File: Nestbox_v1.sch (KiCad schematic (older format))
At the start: 33 parts, among them P1 RX/TX, P2 TST/RST, P3 VDD/GND, Q1 SFH 3605, Q2 SFH 3605, SW1 SMD-BUTTON_2P-3.0X2.5X1.2+0.4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, U1 MSP430FR5969, Y1 Crystal

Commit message: updated schematics and BOM with MPN
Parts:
- D1: MPN (none) -> 720-SFH4646Z
- Q1, Q2: MPN (none) -> SFH 3605-Z
- RV1, RV2: MPN (none) -> 3313J-1-201E
- SW1: MPN B3U-1000P-2P-SMD -> B3U-1000P-B
- U1: MPN (none) -> MSP430FR5969IRGZR
- Y1: MPN (none) -> FC-12M 32.7680KA-A3
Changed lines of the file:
@@
 F 2 "chips:S-PVQFN-N48" H 4500 3500 60  0001 C CNN
 F 3 "" H 4500 3500 60  0001 C CNN
+F 4 "MSP430FR5969IRGZR" H 4500 3500 60  0001 C CNN "MPN"
+F 5 "" H 4500 3500 60  0001 C CNN "SKU"
+F 6 "" H 4500 3500 60  0001 C CNN "MouserLink"
 	1    4450 3650
 	1    0    0    -1
@@
 F 2 "Socket_Strips:Socket_Strip_Straight_1x02" H 5650 6450 50  0001 C CNN
 F 3 "" H 5650 6450 50  0000 C CNN
+F 4 "" H 5650 6450 50  0001 C CNN "MPN"
+F 5 "" H 5650 6450 50  0001 C CNN "SKU"
+F 6 "" H 5650 6450 50  0001 C CNN "MouserLink"
 	1    5650 6450
 	0    1    1    0
@@
 F 2 "SeeedOPL-Crystal Oscillator-2016:X2-SMD-L2.0X1.2X0.55MM" H 4150 1300 50  0001 C CNN
 F 3 "" H 4150 1300 50  0000 C CNN
+F 4 "FC-12M 32.7680KA-A3" H 4150 1300 50  0001 C CNN "MPN"
+F 5 "" H 4150 1300 50  0001 C CNN "SKU"
+F 6 "" H 4150 1300 50  0001 C CNN "MouserLink"
 	1    4150 1300
 	1    0    0    -1
@@
 F 3 "" H 3550 1350 60  0001 C CNN
 F 4 "303030020" H 3580 1500 20  0001 C CNN "SKU"
+F 6 "" H 3580 1500 20  0001 C CNN "" "MouserLink"
 	1    3550 1350
 	0    -1   -1   0
@@
 F 2 "Octanis3:MIDLED" H 650 4250 50  0001 C CNN
 F 3 "" H 650 4250 50  0000 C CNN
+F 4 "720-SFH4646Z" H 650 4250 50  0001 C CNN "MPN"
+F 5 "" H 650 4250 50  0001 C CNN "SKU"
+F 6 "" H 650 4250 50  0001 C CNN "MouserLink"
 	1    650  4250
 	0    -1   -1   0
@@
 F 4 "RC0603JR-07100RL" H 680 3450 20  0001 C CNN "MPN"
 F 5 "301010090" H 680 3450 20  0001 C CNN "SKU"
+F 6 "" H 680 3450 20  0001 C CNN "" "MouserLink"
 	1    650  3300
 	0    1    1    0
@@
 F 2 "Resistors_SMD:R_0603" V 980 3800 50  0001 C CNN
 F 3 "" H 1050 3800 50  0000 C CNN
+F 4 "" H 1050 3800 50  0001 C CNN "MPN"
+F 5 "" H 1050 3800 50  0001 C CNN "SKU"
+F 6 "" H 1050 3800 50  0001 C CNN "MouserLink"
 	1    1050 3800
 	1    0    0    -1
@@
 F 2 "Octanis3:MIDLED_phototransistor" H 950 4350 50  0001 C CNN
 F 3 "" H 950 4350 50  0000 C CNN
+F 4 "SFH 3605-Z" H 950 4350 50  0001 C CNN "MPN"
+F 5 "" H 950 4350 50  0001 C CNN "SKU"
+F 6 "" H 950 4350 50  0001 C CNN "MouserLink"
 	1    950  4350
 	1    0    0    -1
@@
 F 2 "Resistors_SMD:R_0603" V 1980 4100 50  0001 C CNN
 F 3 "" H 2050 4100 50  0000 C CNN
+F 4 "" H 2050 4100 50  0001 C CNN "MPN"
+F 5 "" H 2050 4100 50  0001 C CNN "SKU"
+F 6 "" H 2050 4100 50  0001 C CNN "MouserLink"
 	1    2050 4100
 	0    1    1    0
@@
 F 2 "pot:3223G" H 1400 3800 50  0001 C CNN
 F 3 "" H 1400 3800 50  0000 C CNN
+F 4 "3313J-1-201E" H 1400 3800 50  0001 C CNN "MPN"
+F 5 "" H 1400 3800 50  0001 C CNN "SKU"
+F 6 "" H 1400 3800 50  0001 C CNN "MouserLink"
 	1    1400 3800
 	-1   0    0    1
@@
 F 2 "Resistors_SMD:R_0603" V 1680 3800 50  0001 C CNN
 F 3 "" H 1750 3800 50  0000 C CNN
+F 4 "" H 1750 3800 50  0001 C CNN "MPN"
+F 5 "" H 1750 3800 50  0001 C CNN "SKU"
+F 6 "" H 1750 3800 50  0001 C CNN "MouserLink"
 	1    1750 3800
 	0    -1   -1   0
@@
 F 2 "SeeedOPL-Switch-2016:SW2-2.6-3.0X2.5X1.2+0.4MM" H 4650 6800 60  0001 C CNN
 F 3 "" H 4650 6800 60  0001 C CNN
-F 4 "B3U-1000P-2P-SMD" H 4680 6950 20  0001 C CNN "MPN"
+F 4 "B3U-1000P-B" H 4680 6950 20  0001 C CNN "MPN"
 F 5 "311020047" H 4680 6950 20  0001 C CNN "SKU"
+F 6 "" H 4680 6950 20  0001 C CNN "" "MouserLink"
 	1    4650 6800
 	0    1    1    0
@@
 F 4 "RC0603JR-071KL" H 4030 6850 20  0001 C CNN "MPN"
 F 5 "301010291" H 4030 6850 20  0001 C CNN "SKU"
+F 6 "" H 4030 6850 20  0001 C CNN "" "MouserLink"
 	1    4000 6700
 	0    1    1    0
@@
 F 4 "RC0603JR-071KL" H 4330 6850 20  0001 C CNN "MPN"
 F 5 "301010291" H 4330 6850 20  0001 C CNN "SKU"
+F 6 "" H 4330 6850 20  0001 C CNN "" "MouserLink"
 	1    4300 6700
 	0    1    1    0
@@
 F 4 "RC0603FR-0710KL" H 4680 7500 20  0001 C CNN "MPN"
 F 5 "301010299" H 4680 7500 20  0001 C CNN "SKU"
+F 6 "" H 4680 7500 20  0001 C CNN "" "MouserLink"
 	1    4650 7350
 	0    1    1    0
@@
 F 2 "Socket_Strips:Socket_Strip_Straight_1x02" H 5250 6450 50  0001 C CNN
 F 3 "" H 5250 6450 50  0000 C CNN
+F 4 "" H 5250 6450 50  0001 C CNN "MPN"
+F 5 "" H 5250 6450 50  0001 C CNN "SKU"
+F 6 "" H 5250 6450 50  0001 C CNN "MouserLink"
 	1    5250 6450
 	0    1    1    0
@@
 F 2 "Socket_Strips:Socket_Strip_Straight_1x02" H 6150 6500 50  0001 C CNN
 F 3 "" H 6150 6500 50  0000 C CNN
+F 4 "" H 6150 6500 50  0001 C CNN "MPN"
+F 5 "" H 6150 6500 50  0001 C CNN "SKU"
+F 6 "" H 6150 6500 50  0001 C CNN "MouserLink"
 	1    6150 6500
 	0    1    1    0
@@
 F 4 "CC0603JRNPO9BN120" H 4380 1300 20  0001 C CNN "MPN"
 F 5 "302010067" H 4380 1300 20  0001 C CNN "SKU"
+F 6 "" H 4380 1300 20  0001 C CNN "" "MouserLink"
 	1    4350 1150
 	0    -1   -1   0
@@
 F 4 "CC0603JRNPO9BN120" H 3930 1300 20  0001 C CNN "MPN"
 F 5 "302010067" H 3930 1300 20  0001 C CNN "SKU"
+F 6 "" H 3930 1300 20  0001 C CNN "" "MouserLink"
 	1    3900 1150
 	0    -1   -1   0
@@
 F 4 "CC0603KRX7R9BB104" H 5230 1700 20  0001 C CNN "MPN"
 F 5 "302010138" H 5230 1700 20  0001 C CNN "SKU"
+F 6 "" H 5230 1700 20  0001 C CNN "" "MouserLink"
 	1    5200 1550
 	1    0    0    -1
@@
 F 4 "CC0603KRX7R9BB104" H 3380 1750 20  0001 C CNN "MPN"
 F 5 "302010138" H 3380 1750 20  0001 C CNN "SKU"
+F 6 "" H 3380 1750 20  0001 C CNN "" "MouserLink"
 	1    3350 1600
 	-1   0    0    1
@@
 F 4 "19-217-G7C-AN1P2-3T" H 4030 6500 20  0001 C CNN "MPN"
 F 5 "304090043" H 4030 6500 20  0001 C CNN "SKU"
+F 6 "" H 4030 6500 20  0001 C CNN "" "MouserLink"
 	1    4000 6350
 	0    1    1    0
@@
 F 4 "19-217-BHC-ZL1M2RY-3T" H 4330 6500 20  0001 C CNN "MPN"
 F 5 "304090045" H 4330 6500 20  0001 C CNN "SKU"
+F 6 "" H 4330 6500 20  0001 C CNN "" "MouserLink"
 	1    4300 6350
 	0    1    1    0
@@
 F 4 "CC0805KKX5R8BB106" H 5180 1900 20  0001 C CNN "MPN"
 F 5 "302010178" H 5180 1900 20  0001 C CNN "SKU"
+F 6 "" H 5180 1900 20  0001 C CNN "" "MouserLink"
 	1    5150 1750
 	1    0    0    -1
@@
 F 2 "Socket_Strips:Socket_Strip_Straight_1x02" H 950 3300 50  0001 C CNN
 F 3 "" H 950 3300 50  0000 C CNN
+F 4 "" H 950 3300 50  0001 C CNN "MPN"
+F 5 "" H 950 3300 50  0001 C CNN "SKU"
+F 6 "" H 950 3300 50  0001 C CNN "MouserLink"
 	1    950  3300
 	-1   0    0    1
@@
 F 3 "" H 5900 5950 40  0001 C CNN
 F 4 "FHCFR-1_4W-473J" H 5930 6100 20  0001 C CNN "MPN"
+F 5 "" H 5930 6100 20  0001 C CNN "" "SKU"
+F 6 "" H 5930 6100 20  0001 C CNN "" "MouserLink"
 	1    5900 5950
 	1    0    0    -1
@@
 F 2 "Socket_Strips:Socket_Strip_Straight_1x02" H 1500 4650 50  0001 C CNN
 F 3 "" H 1500 4650 50  0000 C CNN
+F 4 "" H 1500 4650 50  0001 C CNN "MPN"
+F 5 "" H 1500 4650 50  0001 C CNN "SKU"
+F 6 "" H 1500 4650 50  0001 C CNN "MouserLink"
 	1    1500 4650
 	-1   0    0    1
@@
 F 2 "Octanis3:MIDLED_phototransistor" H 750 6050 50  0001 C CNN
 F 3 "" H 750 6050 50  0000 C CNN
+F 4 "SFH 3605-Z" H 750 6050 50  0001 C CNN "MPN"
+F 5 "" H 750 6050 50  0001 C CNN "SKU"
+F 6 "" H 750 6050 50  0001 C CNN "MouserLink"
 	1    750  6050
 	1    0    0    -1
@@
 F 2 "Resistors_SMD:R_0603" V 780 5600 50  0001 C CNN
 F 3 "" H 850 5600 50  0000 C CNN
+F 4 "" H 850 5600 50  0001 C CNN "MPN"
+F 5 "" H 850 5600 50  0001 C CNN "SKU"
+F 6 "" H 850 5600 50  0001 C CNN "MouserLink"
 	1    850  5600
 	1    0    0    -1
@@
 F 2 "pot:3223G" H 1350 5550 50  0001 C CNN
 F 3 "" H 1350 5550 50  0000 C CNN
+F 4 "3313J-1-201E" H 1350 5550 50  0001 C CNN "MPN"
+F 5 "" H 1350 5550 50  0001 C CNN "SKU"
+F 6 "" H 1350 5550 50  0001 C CNN "MouserLink"
 	1    1350 5550
 	-1   0    0    1
@@
 F 2 "Resistors_SMD:R_0603" V 1730 5550 50  0001 C CNN
 F 3 "" H 1800 5550 50  0000 C CNN
+F 4 "" H 1800 5550 50  0001 C CNN "MPN"
+F 5 "" H 1800 5550 50  0001 C CNN "SKU"
+F 6 "" H 1800 5550 50  0001 C CNN "MouserLink"
 	1    1800 5550
 	0    -1   -1   0
@@
 F 4 "RC0603FR-0710KL" H 4980 7300 20  0001 C CNN "MPN"
 F 5 "301010299" H 4980 7300 20  0001 C CNN "SKU"
+F 6 "" H 4980 7300 20  0001 C CNN "" "MouserLink"
 	1    4950 7150
 	1    0    0    -1
@@
 F 4 "CC0603KRX7R9BB104" H 5430 7200 20  0001 C CNN "MPN"
 F 5 "302010138" H 5430 7200 20  0001 C CNN "SKU"
+F 6 "" H 5430 7200 20  0001 C CNN "" "MouserLink"
 	1    5400 7050
 	1    0    0    -1

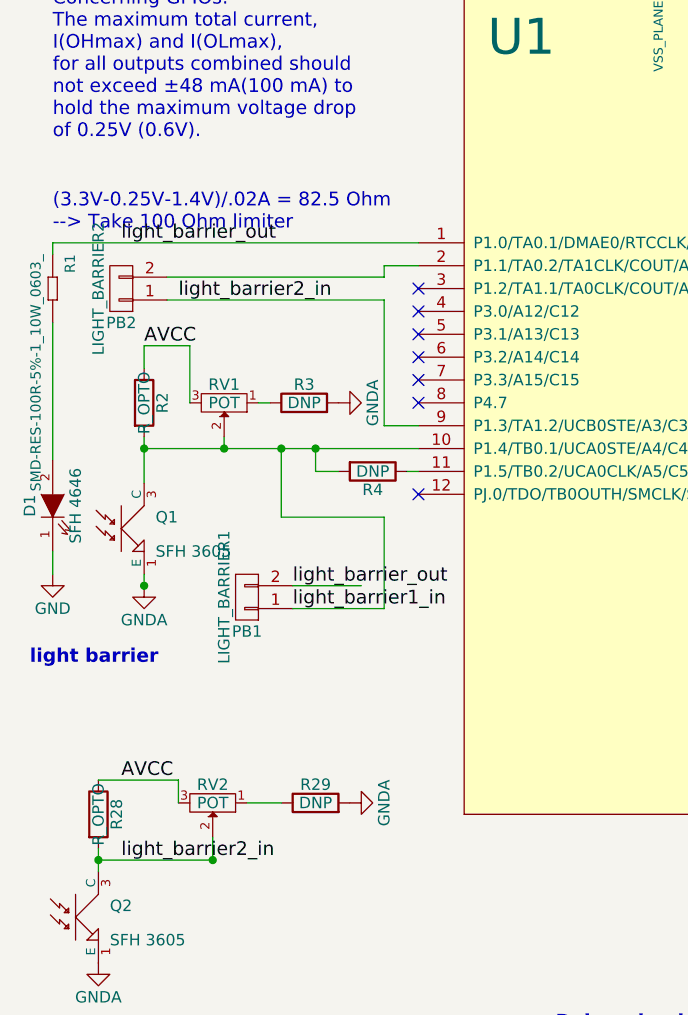
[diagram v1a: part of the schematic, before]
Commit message: Updated BOM with correct light barrier values
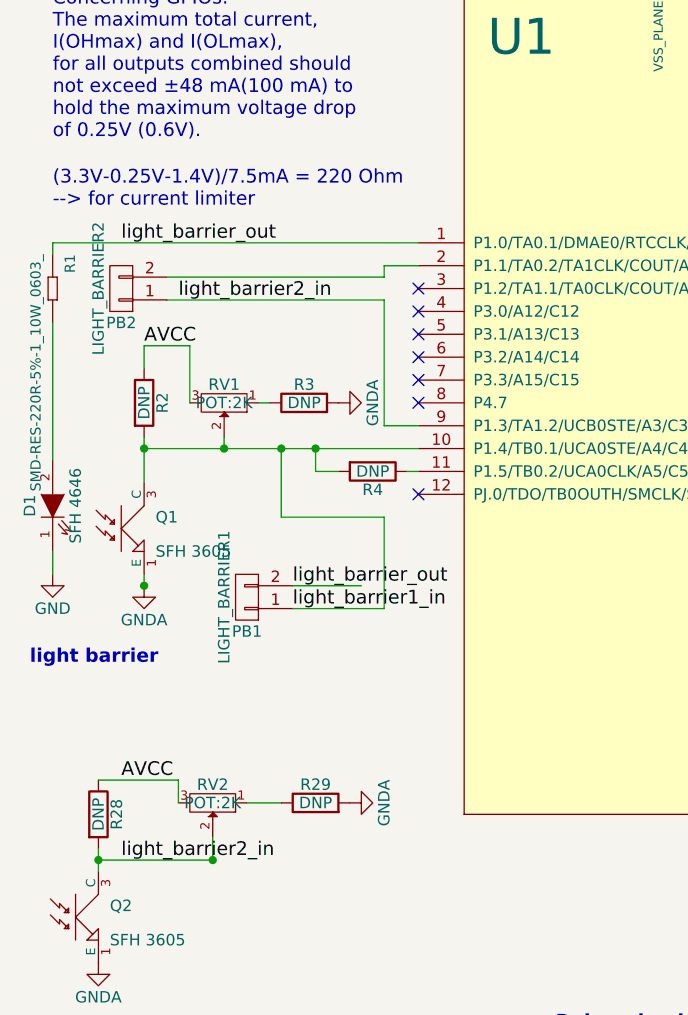
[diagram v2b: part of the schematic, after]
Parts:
- removed R1: SMD-RES-100R-5%-1_10W_0603_, SeeedOPL-Resistor-2016:R0603, symbol SMD-RES-100R-5%-1_10W_0603_
- added R1: SMD-RES-220R-5%-1_10W_0603_, symbol SMD-RES-220R-5%-1_10W_0603_
- R2, R28: value R_OPTO -> DNP
- RV1, RV2: value POT -> POT:2K
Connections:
- net light_barrier_out: now also R1.1
- net at D1.2 (A): now also R1.2
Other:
- note added: "(3.3V-0.25V-1.4V)/7.5mA = 220 Ohm\n--> for current limiter"
- note removed: "(3.3V-0.25V-1.4V)/.02A = 82.5 Ohm\n--> Take 100 Ohm limiter\n"
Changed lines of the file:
@@
 F 3 "" H 3550 1350 60  0001 C CNN
 F 4 "303030020" H 3580 1500 20  0001 C CNN "SKU"
-F 6 "" H 3580 1500 20  0001 C CNN "" "MouserLink"
+F 5 "" H 3580 1500 20  0001 C CNN "Field6"
 	1    3550 1350
 	0    -1   -1   0
@@
 	1    0    0    -1
 $EndComp
-Text Notes 650  3050 0    60   ~ 0
-(3.3V-0.25V-1.4V)/.02A = 82.5 Ohm\n--> Take 100 Ohm limiter\n
-$Comp
-L SMD-RES-100R-5%-1_10W_0603_ R1
-U 1 1 587A75A7
-P 650 3300
-F 0 "R1" H 500 3350 45  0000 L BNN
-F 1 "SMD-RES-100R-5%-1_10W_0603_" H 500 3200 45  0000 L BNN
-F 2 "SeeedOPL-Resistor-2016:R0603" H 650 3300 40  0001 C CNN
-F 3 "" H 650 3300 40  0001 C CNN
-F 4 "RC0603JR-07100RL" H 680 3450 20  0001 C CNN "MPN"
-F 5 "301010090" H 680 3450 20  0001 C CNN "SKU"
-F 6 "" H 680 3450 20  0001 C CNN "" "MouserLink"
-	1    650  3300
-	0    1    1    0
-$EndComp
+Text Notes 650  2950 0    60   ~ 0
+(3.3V-0.25V-1.4V)/7.5mA = 220 Ohm\n--> for current limiter
 $Comp
 L R R2
@@
 P 1050 3800
 F 0 "R2" V 1130 3800 50  0000 C CNN
-F 1 "R_OPTO" V 1050 3800 50  0000 C CNN
+F 1 "DNP" V 1050 3800 50  0000 C CNN
 F 2 "Resistors_SMD:R_0603" V 980 3800 50  0001 C CNN
 F 3 "" H 1050 3800 50  0000 C CNN
@@
 P 1400 3800
 F 0 "RV1" H 1400 3720 50  0000 C CNN
-F 1 "POT" H 1400 3800 50  0000 C CNN
+F 1 "POT:2K" H 1400 3800 50  0000 C CNN
 F 2 "pot:3223G" H 1400 3800 50  0001 C CNN
 F 3 "" H 1400 3800 50  0000 C CNN
@@
 F 4 "B3U-1000P-B" H 4680 6950 20  0001 C CNN "MPN"
 F 5 "311020047" H 4680 6950 20  0001 C CNN "SKU"
-F 6 "" H 4680 6950 20  0001 C CNN "" "MouserLink"
+F 6 "" H 4680 6950 20  0001 C CNN "Field6"
 	1    4650 6800
 	0    1    1    0
@@
 F 4 "RC0603JR-071KL" H 4030 6850 20  0001 C CNN "MPN"
 F 5 "301010291" H 4030 6850 20  0001 C CNN "SKU"
-F 6 "" H 4030 6850 20  0001 C CNN "" "MouserLink"
+F 6 "" H 4030 6850 20  0001 C CNN "Field6"
 	1    4000 6700
 	0    1    1    0
@@
 F 4 "RC0603JR-071KL" H 4330 6850 20  0001 C CNN "MPN"
 F 5 "301010291" H 4330 6850 20  0001 C CNN "SKU"
-F 6 "" H 4330 6850 20  0001 C CNN "" "MouserLink"
+F 6 "" H 4330 6850 20  0001 C CNN "Field6"
 	1    4300 6700
 	0    1    1    0
@@
 F 4 "RC0603FR-0710KL" H 4680 7500 20  0001 C CNN "MPN"
 F 5 "301010299" H 4680 7500 20  0001 C CNN "SKU"
-F 6 "" H 4680 7500 20  0001 C CNN "" "MouserLink"
+F 6 "" H 4680 7500 20  0001 C CNN "Field6"
 	1    4650 7350
 	0    1    1    0
@@
 F 4 "CC0603JRNPO9BN120" H 4380 1300 20  0001 C CNN "MPN"
 F 5 "302010067" H 4380 1300 20  0001 C CNN "SKU"
-F 6 "" H 4380 1300 20  0001 C CNN "" "MouserLink"
+F 6 "" H 4380 1300 20  0001 C CNN "Field6"
 	1    4350 1150
 	0    -1   -1   0
@@
 F 4 "CC0603JRNPO9BN120" H 3930 1300 20  0001 C CNN "MPN"
 F 5 "302010067" H 3930 1300 20  0001 C CNN "SKU"
-F 6 "" H 3930 1300 20  0001 C CNN "" "MouserLink"
+F 6 "" H 3930 1300 20  0001 C CNN "Field6"
 	1    3900 1150
 	0    -1   -1   0
@@
 F 4 "CC0603KRX7R9BB104" H 5230 1700 20  0001 C CNN "MPN"
 F 5 "302010138" H 5230 1700 20  0001 C CNN "SKU"
-F 6 "" H 5230 1700 20  0001 C CNN "" "MouserLink"
+F 6 "" H 5230 1700 20  0001 C CNN "Field6"
 	1    5200 1550
 	1    0    0    -1
@@
 F 4 "CC0603KRX7R9BB104" H 3380 1750 20  0001 C CNN "MPN"
 F 5 "302010138" H 3380 1750 20  0001 C CNN "SKU"
-F 6 "" H 3380 1750 20  0001 C CNN "" "MouserLink"
+F 6 "" H 3380 1750 20  0001 C CNN "Field6"
 	1    3350 1600
 	-1   0    0    1
@@
 F 4 "19-217-G7C-AN1P2-3T" H 4030 6500 20  0001 C CNN "MPN"
 F 5 "304090043" H 4030 6500 20  0001 C CNN "SKU"
-F 6 "" H 4030 6500 20  0001 C CNN "" "MouserLink"
+F 6 "" H 4030 6500 20  0001 C CNN "Field6"
 	1    4000 6350
 	0    1    1    0
@@
 F 4 "19-217-BHC-ZL1M2RY-3T" H 4330 6500 20  0001 C CNN "MPN"
 F 5 "304090045" H 4330 6500 20  0001 C CNN "SKU"
-F 6 "" H 4330 6500 20  0001 C CNN "" "MouserLink"
+F 6 "" H 4330 6500 20  0001 C CNN "Field6"
 	1    4300 6350
 	0    1    1    0
@@
 F 4 "CC0805KKX5R8BB106" H 5180 1900 20  0001 C CNN "MPN"
 F 5 "302010178" H 5180 1900 20  0001 C CNN "SKU"
-F 6 "" H 5180 1900 20  0001 C CNN "" "MouserLink"
+F 6 "" H 5180 1900 20  0001 C CNN "Field6"
 	1    5150 1750
 	1    0    0    -1
@@
 F 3 "" H 5900 5950 40  0001 C CNN
 F 4 "FHCFR-1_4W-473J" H 5930 6100 20  0001 C CNN "MPN"
-F 5 "" H 5930 6100 20  0001 C CNN "" "SKU"
-F 6 "" H 5930 6100 20  0001 C CNN "" "MouserLink"
+F 5 "" H 5930 6100 20  0001 C CNN "Field5"
+F 6 "" H 5930 6100 20  0001 C CNN "Field6"
 	1    5900 5950
 	1    0    0    -1
@@
 P 850 5600
 F 0 "R28" V 930 5600 50  0000 C CNN
-F 1 "R_OPTO" V 850 5600 50  0000 C CNN
+F 1 "DNP" V 850 5600 50  0000 C CNN
 F 2 "Resistors_SMD:R_0603" V 780 5600 50  0001 C CNN
 F 3 "" H 850 5600 50  0000 C CNN
@@
 P 1350 5550
 F 0 "RV2" H 1350 5470 50  0000 C CNN
-F 1 "POT" H 1350 5550 50  0000 C CNN
+F 1 "POT:2K" H 1350 5550 50  0000 C CNN
 F 2 "pot:3223G" H 1350 5550 50  0001 C CNN
 F 3 "" H 1350 5550 50  0000 C CNN
@@
 F 4 "RC0603FR-0710KL" H 4980 7300 20  0001 C CNN "MPN"
 F 5 "301010299" H 4980 7300 20  0001 C CNN "SKU"
-F 6 "" H 4980 7300 20  0001 C CNN "" "MouserLink"
+F 6 "" H 4980 7300 20  0001 C CNN "Field6"
 	1    4950 7150
 	1    0    0    -1
@@
 F 4 "CC0603KRX7R9BB104" H 5430 7200 20  0001 C CNN "MPN"
 F 5 "302010138" H 5430 7200 20  0001 C CNN "SKU"
-F 6 "" H 5430 7200 20  0001 C CNN "" "MouserLink"
+F 6 "" H 5430 7200 20  0001 C CNN "Field6"
 	1    5400 7050
 	1    0    0    -1
@@
 Wire Wire Line
 	5550 7050 5650 7050
+$Comp
+L SMD-RES-220R-5%-1_10W_0603_ R1
+U 1 1 58E30C83
+P 650 3300
+F 0 "R1" H 500 3350 45  0000 L BNN
+F 1 "SMD-RES-220R-5%-1_10W_0603_" H 500 3200 45  0000 L BNN
+F 2 "" H 650 3300 40  0001 C CNN
+F 3 "" H 650 3300 40  0001 C CNN
+F 4 "RC0603JR-07220RL" H 680 3450 20  0001 C CNN "MPN"
+F 5 "301010163" H 680 3450 20  0001 C CNN "SKU"
+	1    650  3300
+	0    1    1    0
+$EndComp
 $EndSCHEMATC

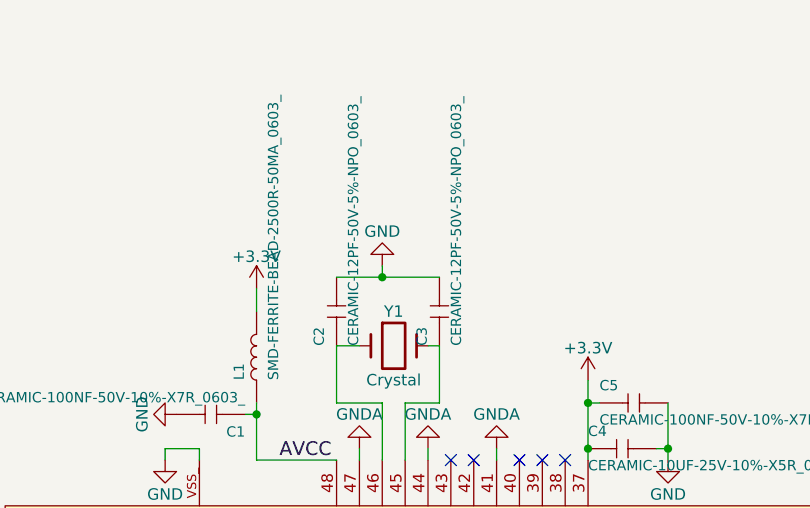
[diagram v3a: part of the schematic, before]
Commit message: added feedback of first soldering round (3pcs)
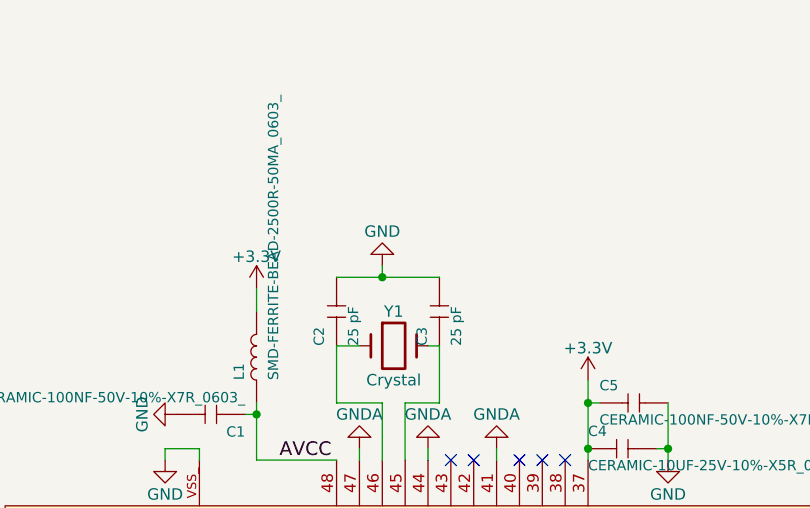
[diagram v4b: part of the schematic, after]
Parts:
- C2, C3: value CERAMIC-12PF-50V-5%-NPO_0603_ -> 25 pF
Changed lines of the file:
@@
 P 4350 1150
 F 0 "C3" H 4200 1200 45  0000 L BNN
-F 1 "CERAMIC-12PF-50V-5%-NPO_0603_" H 4200 1050 45  0000 L BNN
+F 1 "25 pF" H 4200 1050 45  0000 L BNN
 F 2 "SeeedOPL-Capacitor-2016:C0603" H 4350 1150 60  0001 C CNN
 F 3 "" H 4350 1150 60  0001 C CNN
@@
 P 3900 1150
 F 0 "C2" H 3750 1200 45  0000 L BNN
-F 1 "CERAMIC-12PF-50V-5%-NPO_0603_" H 3750 1050 45  0000 L BNN
+F 1 "25 pF" H 3750 1050 45  0000 L BNN
 F 2 "SeeedOPL-Capacitor-2016:C0603" H 3900 1150 60  0001 C CNN
 F 3 "" H 3900 1150 60  0001 C CNN
